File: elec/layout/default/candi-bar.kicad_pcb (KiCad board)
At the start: 4 copper layers, 88 x 44 mm, 67 parts, among them J1 ?, J2 ?, J3 ?, J4 ?, J5 ?, J6 ?, J7 ?, U1 ?, U10 ?, U11 ?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

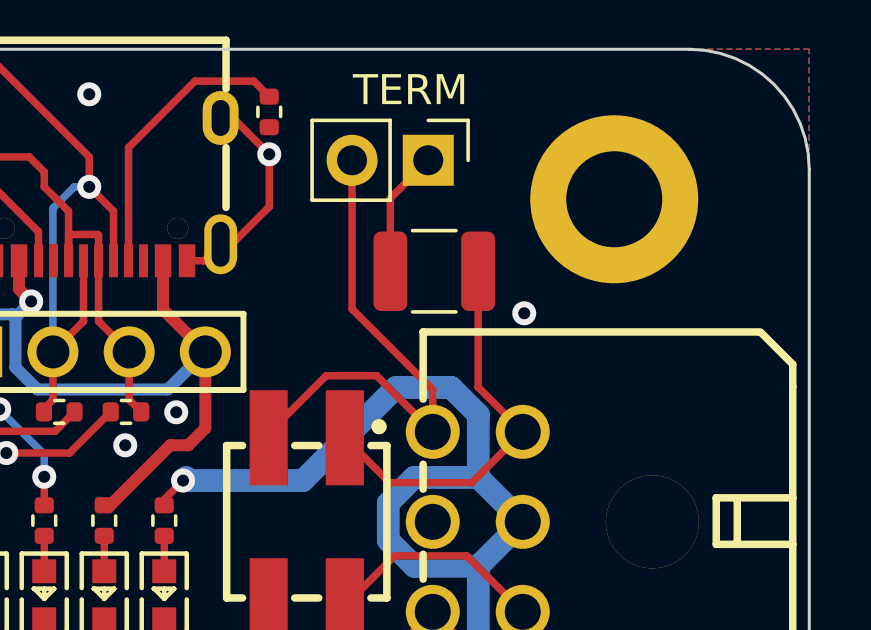
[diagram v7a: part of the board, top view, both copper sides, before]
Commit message: feat: Switch termination resistor to 1206 to use basic part
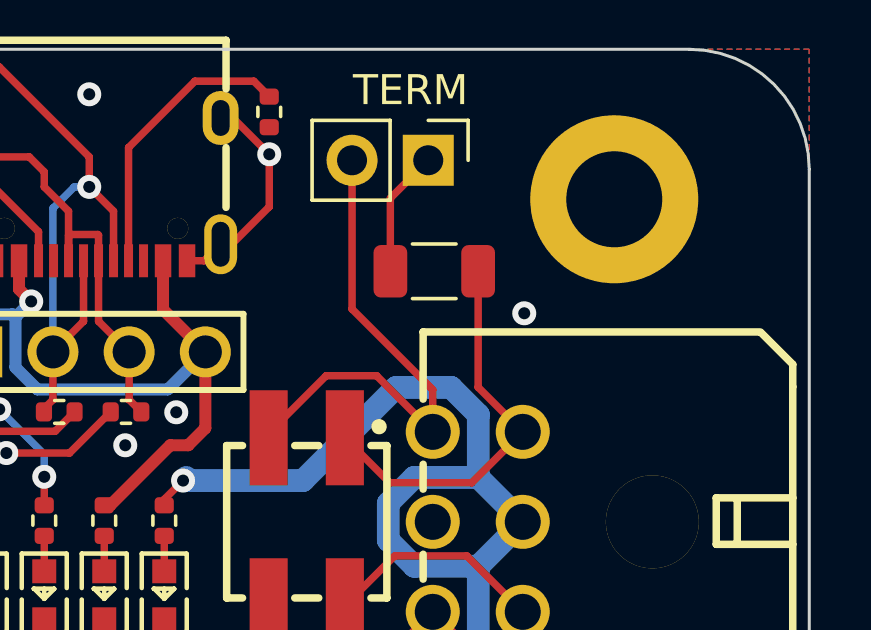
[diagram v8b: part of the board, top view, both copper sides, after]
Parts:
- R16: value 333.333mW Thick Film Resistors 200V ±100ppm/℃ ±1% 120Ω 1210 Chip Resistor - Surface Mount ROHS -> 250mW Thick Film Resistors 200V ±100ppm/℃ ±1% 120Ω 1206 Chip Resistor - Surface Mount ROHS; footprint lib:R1210 -> lib:R1206
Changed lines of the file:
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@@
 		)
 	)
-	(footprint "lib:R1210"
+	(footprint "lib:R1206"
 		(layer "F.Cu")
 		(at 169 63.4 180)
-		(descr "Resistor SMD 1210 (3225 Metric), square (rectangular) end terminal, IPC_7351 nominal, (Body size source: IPC-SM-782 page 72, https://www.pcb-3d.com/wordpress/wp-content/uploads/ipc-sm-782a_amendment_1_and_2.pdf), generated with kicad-footprint-generator")
+		(descr "Resistor SMD 1206 (3216 Metric), square (rectangular) end terminal, IPC_7351 nominal, (Body size source: IPC-SM-782 page 72, https://www.pcb-3d.com/wordpress/wp-content/uploads/ipc-sm-782a_amendment_1_and_2.pdf), generated with kicad-footprint-generator")
 		(tags "resistor")
 		(property "Reference" "R16"
-			(at 0 -2.28 180)
+			(at 0 -1.82 180)
 			(layer "F.SilkS")
 			(hide yes)
@@
 			)
 		)
-		(property "Value" "333.333mW Thick Film Resistors 200V ±100ppm/℃ ±1% 120Ω 1210  Chip Resistor - Surface Mount ROHS"
-			(at 0 2.28 180)
+		(property "Value" "250mW Thick Film Resistors 200V ±100ppm/℃ ±1% 120Ω 1206 Chip Resistor - Surface Mount ROHS"
+			(at 0 1.82 180)
 			(layer "F.Fab")
 			(effects
@@
 		(attr smd)
 		(fp_line
-			(start -0.723737 1.355)
-			(end 0.723737 1.355)
+			(start -0.727064 0.91)
+			(end 0.727064 0.91)
 			(stroke
 				(width 0.12)
@@
 		)
 		(fp_line
-			(start -0.723737 -1.355)
-			(end 0.723737 -1.355)
+			(start -0.727064 -0.91)
+			(end 0.727064 -0.91)
 			(stroke
 				(width 0.12)
@@
 		)
 		(fp_line
-			(start 2.28 1.58)
-			(end -2.28 1.58)
+			(start 2.28 1.12)
+			(end -2.28 1.12)
 			(stroke
 				(width 0.05)
@@
 		)
 		(fp_line
-			(start 2.28 -1.58)
-			(end 2.28 1.58)
+			(start 2.28 -1.12)
+			(end 2.28 1.12)
 			(stroke
 				(width 0.05)
@@
 		)
 		(fp_line
-			(start -2.28 1.58)
-			(end -2.28 -1.58)
+			(start -2.28 1.12)
+			(end -2.28 -1.12)
 			(stroke
 				(width 0.05)
@@
 		)
 		(fp_line
-			(start -2.28 -1.58)
-			(end 2.28 -1.58)
+			(start -2.28 -1.12)
+			(end 2.28 -1.12)
 			(stroke
 				(width 0.05)
@@
 		)
 		(fp_line
-			(start 1.6 1.245)
-			(end -1.6 1.245)
+			(start 1.6 0.8)
+			(end -1.6 0.8)
 			(stroke
 				(width 0.1)
@@
 		)
 		(fp_line
-			(start 1.6 -1.245)
-			(end 1.6 1.245)
+			(start 1.6 -0.8)
+			(end 1.6 0.8)
 			(stroke
 				(width 0.1)
@@
 		)
 		(fp_line
-			(start -1.6 1.245)
-			(end -1.6 -1.245)
+			(start -1.6 0.8)
+			(end -1.6 -0.8)
 			(stroke
 				(width 0.1)
@@
 		)
 		(fp_line
-			(start -1.6 -1.245)
-			(end 1.6 -1.245)
+			(start -1.6 -0.8)
+			(end 1.6 -0.8)
 			(stroke
 				(width 0.1)
@@
 		(pad "1" smd roundrect
 			(at -1.4625 0 180)
-			(size 1.125 2.65)
+			(size 1.125 1.75)
 			(layers "F.Cu" "F.Mask" "F.Paste")
 			(roundrect_rratio 0.222222)
@@
 		(pad "2" smd roundrect
 			(at 1.4625 0 180)
-			(size 1.125 2.65)
+			(size 1.125 1.75)
 			(layers "F.Cu" "F.Mask" "F.Paste")
 			(roundrect_rratio 0.222222)
@@
 		)
 		(embedded_fonts no)
-		(model "${KICAD6_3DMODEL_DIR}/Resistor_SMD.3dshapes/R_1210_3225Metric.wrl"
+		(model "${KICAD6_3DMODEL_DIR}/Resistor_SMD.3dshapes/R_1206_3216Metric.wrl"
 			(offset
 				(xyz 0 0 0)
@@
 	)
 	(segment
-		(start 167.5375 63.4)
-		(end 167.5375 60.9625)
+		(start 167.5375 60.9625)
+		(end 167.5375 63.4)
 		(width 0.25)
 		(layer "F.Cu")
@@
 	(segment
 		(start 170.4625 67.265)
-		(end 170.4625 63.4)
+		(end 171.95 68.7525)
 		(width 0.25)
 		(layer "F.Cu")
@@
 	)
 	(segment
-		(start 171.95 68.7525)
-		(end 170.4625 67.265)
+		(start 167.52 70.45)
+		(end 170.2525 70.45)
 		(width 0.25)
 		(layer "F.Cu")
@@
 	)
 	(segment
-		(start 167.52 70.45)
-		(end 170.2525 70.45)
+		(start 170.2525 70.45)
+		(end 171.95 68.7525)
 		(width 0.25)
 		(layer "F.Cu")
@@
 	)
 	(segment
-		(start 170.2525 70.45)
-		(end 171.95 68.7525)
+		(start 170.4625 63.4)
+		(end 170.4625 67.265)
 		(width 0.25)
 		(layer "F.Cu")
